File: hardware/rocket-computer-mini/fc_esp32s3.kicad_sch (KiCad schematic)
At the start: 35 parts, among them SW2 R-667995, U32 ESP32-S3RH2, U33 GD25Q128ESIG, Y3 ABS07-32.768KHZ-T, Y4 ECS-400-10-37B2-CKY-TR

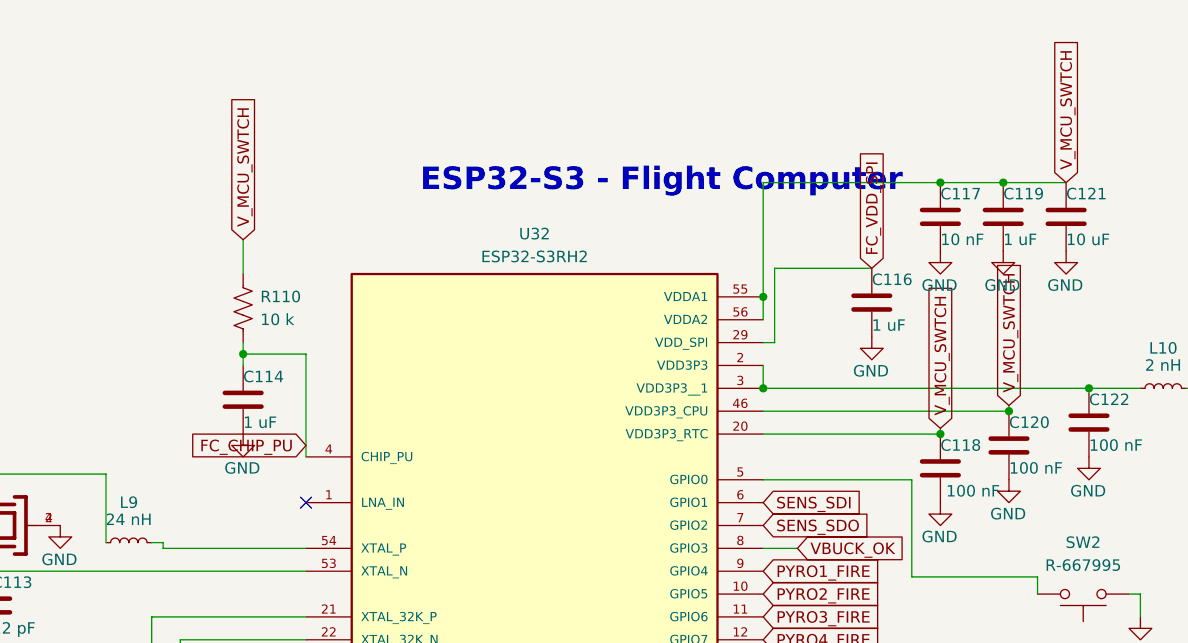
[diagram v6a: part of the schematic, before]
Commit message: rocket-computer-mini: place the board and re-sync the netlist
Placement of all 214 footprints — the import scatter block that sat at x>130 is
gone and everything now falls within x 73.2-124.5 / y 103.7-170.1 mm. The
22.5 x 69.5 mm outline is restored on Edge.Cuts, having gone missing between
0e0f2d5 and 7ad7508 (the pack-direct pyro/supercap WIP commit), which left the
file with no board boundary at all in between.

The stale P4-era track stubs are cleared, and the board is re-synced from the
schematic so its net names finally match: CAP_ACTIVE -> VBUCK_OK and
ARM_CLK -> WDT_PET, plus FC_ARM, OC_ARM_EN and the rest of the arm and TPS61094
hold-up nets. Before this the board file lagged the schematic by two reworks —
9 schematic nets had no PCB counterpart and 3 PCB nets no longer existed — and
kicad-cli pcb drc --schematic-parity did not flag it, because it reconciles
footprints rather than stale net strings.

Not a finished layout: 0 routed segments, 2 vias, 12 zones. DRC reports 103
violations and 372 unconnected pads, which is the expected shape for a placed,
unrouted board.

Taken from the owner's working tree and committed here so the I2S net rename
that follows could be applied on top of it rather than conflicting with it.

Co-Authored-By: Claude Opus 5 <noreply@anthropic.com>
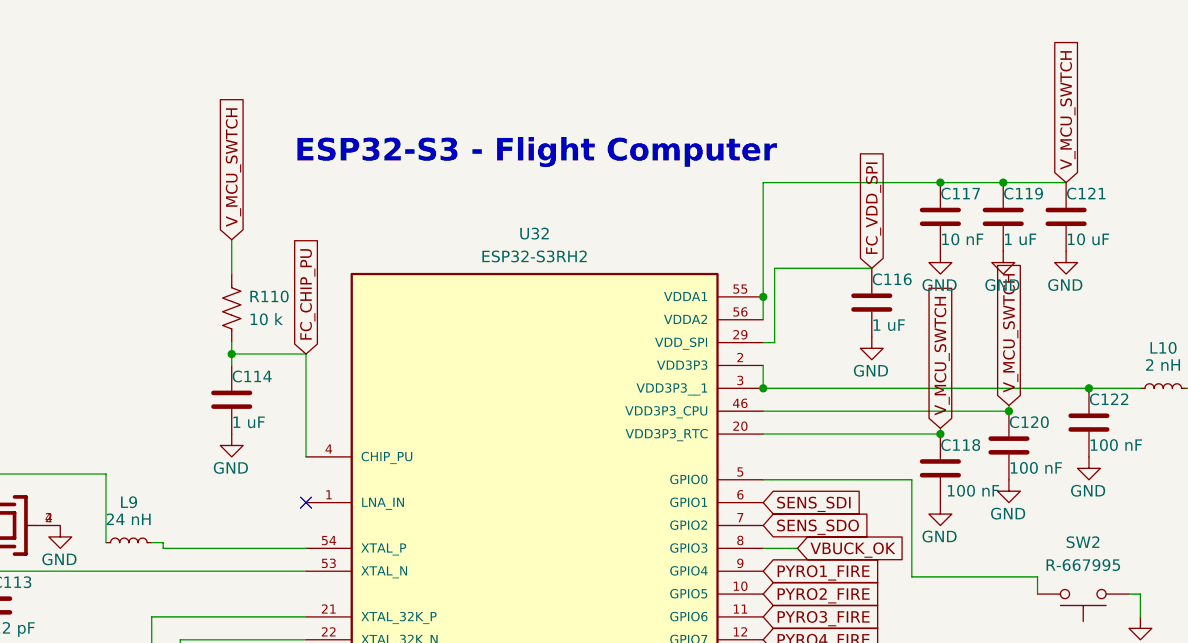
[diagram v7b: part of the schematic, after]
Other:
- moved on the sheet: C114, R110
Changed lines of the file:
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@@
 	(text "ESP32-S3 - Flight Computer"
 		(exclude_from_sim no)
-		(at 151.765 33.02 0)
+		(at 137.795 29.845 0)
 		(effects
 			(font
@@
 	)
 	(junction
-		(at 132.08 50.8)
-		(diameter 0)
-		(color 0 0 0 0)
-	)
-	(junction
 		(at 248.92 54.61)
 		(diameter 0)
@@
 		(color 0 0 0 0)
 	)
+	(junction
+		(at 130.81 50.8)
+		(diameter 0)
+		(color 0 0 0 0)
+	)
 	(no_connect
 		(at 139.065 67.31)
@@
 	(wire
 		(pts
+			(xy 133.985 100.33) (xy 139.065 100.33)
+		)
+		(stroke
+			(width 0)
+			(type default)
+		)
+	)
+	(wire
+		(pts
 			(xy 55.88 118.745) (xy 62.865 118.745)
 		)
@@
 	(wire
 		(pts
-			(xy 132.08 38.1) (xy 132.08 41.91)
+			(xy 130.81 38.1) (xy 130.81 41.91)
 		)
 		(stroke
@@
 	(wire
 		(pts
+			(xy 130.81 50.8) (xy 139.065 50.8)
+		)
+		(stroke
+			(width 0)
+			(type default)
+		)
+	)
+	(wire
+		(pts
 			(xy 189.865 133.35) (xy 193.675 133.35)
 		)
@@
 	(wire
 		(pts
-			(xy 132.08 50.8) (xy 132.08 52.07)
+			(xy 130.81 50.8) (xy 130.81 52.07)
 		)
 		(stroke
@@
 	(wire
 		(pts
+			(xy 139.065 50.8) (xy 139.065 62.23)
+		)
+		(stroke
+			(width 0)
+			(type default)
+		)
+	)
+	(wire
+		(pts
 			(xy 240.03 54.61) (xy 248.92 54.61)
 		)
@@
 	(wire
 		(pts
-			(xy 132.08 49.53) (xy 132.08 50.8)
+			(xy 130.81 49.53) (xy 130.81 50.8)
 		)
 		(stroke
@@
 	(wire
 		(pts
-			(xy 139.065 50.8) (xy 132.08 50.8)
-		)
-		(stroke
-			(width 0)
-			(type default)
-		)
-	)
-	(wire
-		(pts
 			(xy 116.84 64.135) (xy 116.84 71.755)
 		)
@@
 	(wire
 		(pts
-			(xy 139.065 62.23) (xy 139.065 50.8)
-		)
-		(stroke
-			(width 0)
-			(type default)
-		)
-	)
-	(wire
-		(pts
 			(xy 139.065 80.01) (xy 121.92 80.01)
 		)
@@
 		)
 	)
+	(global_label "FC_CHIP_PU"
+		(shape input)
+		(at 139.065 50.8 90)
+		(fields_autoplaced yes)
+		(effects
+			(font
+				(size 1.27 1.27)
+			)
+			(justify left)
+		)
+		(property "Intersheetrefs" "${INTERSHEET_REFS}"
+			(at 139.065 36.4452 90)
+			(hide yes)
+			(show_name no)
+			(do_not_autoplace no)
+			(effects
+				(font
+					(size 1.27 1.27)
+				)
+				(justify left)
+			)
+		)
+	)
+	(global_label "FC_ARM"
+		(shape input)
+		(at 133.985 100.33 180)
+		(fields_autoplaced yes)
+		(effects
+			(font
+				(size 1.27 1.27)
+			)
+			(justify right)
+		)
+		(property "Intersheetrefs" "${INTERSHEET_REFS}"
+			(at 133.985 100.33 0)
+			(hide yes)
+			(show_name no)
+			(do_not_autoplace no)
+			(effects
+				(font
+					(size 1.27 1.27)
+				)
+				(justify right)
+			)
+		)
+	)
 	(global_label "FC_D-"
 		(shape input)
@@
 	(global_label "V_MCU_SWTCH"
 		(shape input)
-		(at 132.08 38.1 90)
+		(at 130.81 38.1 90)
 		(fields_autoplaced yes)
 		(effects
@@
 		)
 		(property "Intersheetrefs" "${INTERSHEET_REFS}"
-			(at 132.08 21.81 90)
+			(at 130.81 21.81 90)
 			(hide yes)
 			(show_name no)
@@
 	(symbol
 		(lib_id "Device:R_US")
-		(at 132.08 45.72 0)
+		(at 130.81 45.72 0)
 		(unit 1)
 		(body_style 1)
@@
 		(fields_autoplaced yes)
 		(property "Reference" "R110"
-			(at 133.985 44.4499 0)
+			(at 132.715 44.4499 0)
 			(show_name no)
 			(do_not_autoplace no)
@@
 		)
 		(property "Value" "10 k"
-			(at 133.985 46.9899 0)
+			(at 132.715 46.9899 0)
 			(show_name no)
 			(do_not_autoplace no)
@@
 		)
 		(property "Footprint" "Resistor_SMD:R_0402_1005Metric"
-			(at 133.096 45.974 90)
+			(at 131.826 45.974 90)
 			(hide yes)
 			(show_name no)
@@
 		)
 		(property "Datasheet" ""
-			(at 132.08 45.72 0)
+			(at 130.81 45.72 0)
 			(hide yes)
 			(show_name no)
@@
 		)
 		(property "Description" "Resistor, US symbol"
-			(at 132.08 45.72 0)
+			(at 130.81 45.72 0)
 			(hide yes)
 			(show_name no)
@@
 		)
 		(property "MPN" "RC0402FR-0710KL"
-			(at 132.08 45.72 0)
+			(at 130.81 45.72 0)
 			(hide yes)
 			(show_name no)
@@
 		)
 		(property "Mfr" "Yageo"
-			(at 132.08 45.72 0)
+			(at 130.81 45.72 0)
 			(hide yes)
 			(show_name no)
@@
 	(symbol
 		(lib_id "Device:C")
-		(at 132.08 55.88 0)
+		(at 130.81 55.88 0)
 		(unit 1)
 		(body_style 1)
@@
 		(dnp no)
 		(property "Reference" "C114"
-			(at 132.08 53.34 0)
+			(at 130.81 53.34 0)
 			(show_name no)
 			(do_not_autoplace no)
@@
 		)
 		(property "Value" "1 uF"
-			(at 132.08 58.42 0)
+			(at 130.81 58.42 0)
 			(show_name no)
 			(do_not_autoplace no)
@@
 		)
 		(property "Footprint" "Capacitor_SMD:C_0402_1005Metric"
-			(at 133.0452 59.69 0)
+			(at 131.7752 59.69 0)
 			(hide yes)
 			(show_name no)
@@
 		)
 		(property "Datasheet" ""
-			(at 132.08 55.88 0)
+			(at 130.81 55.88 0)
 			(hide yes)
 			(show_name no)
@@
 		)
 		(property "Description" "Unpolarized capacitor"
-			(at 132.08 55.88 0)
+			(at 130.81 55.88 0)
 			(hide yes)
 			(show_name no)
@@
 		)
 		(property "MPN" "CL05A105KO5NNNC"
-			(at 132.08 55.88 0)
+			(at 130.81 55.88 0)
 			(hide yes)
 			(show_name no)
@@
 		)
 		(property "Mfr" "Samsung"
-			(at 132.08 55.88 0)
+			(at 130.81 55.88 0)
 			(hide yes)
 			(show_name no)
@@
 	(symbol
 		(lib_id "power:GND")
-		(at 132.08 59.69 0)
+		(at 130.81 59.69 0)
 		(unit 1)
 		(body_style 1)
@@
 		(dnp no)
 		(property "Reference" "#PWR0311"
-			(at 132.08 66.04 0)
+			(at 130.81 66.04 0)
 			(hide yes)
 			(show_name no)
@@
 		)
 		(property "Value" "GND"
-			(at 133.985 63.5 0)
+			(at 132.715 63.5 0)
 			(show_name no)
 			(do_not_autoplace no)
@@
 		)
 		(property "Footprint" ""
-			(at 132.08 59.69 0)
+			(at 130.81 59.69 0)
 			(hide yes)
 			(show_name no)
@@
 		)
 		(property "Datasheet" ""
-			(at 132.08 59.69 0)
+			(at 130.81 59.69 0)
 			(hide yes)
 			(show_name no)
@@
 		)
 		(property "Description" "Power symbol creates a global label with name \"GND\" , ground"
-			(at 132.08 59.69 0)
+			(at 130.81 59.69 0)
 			(hide yes)
 			(show_name no)
@@
 			)
 		)
-	)
-	(wire
-		(pts
-			(xy 133.985 100.33) (xy 139.065 100.33)
-		)
-		(stroke
-			(width 0)
-			(type default)
-		)
-	)
-	(global_label "FC_ARM"
-		(shape input)
-		(at 133.985 100.33 180)
-		(fields_autoplaced yes)
-		(effects
-			(font
-				(size 1.27 1.27)
-			)
-			(justify right)
-		)
-		(property "Intersheetrefs" "${INTERSHEET_REFS}"
-			(at 133.985 100.33 0)
-			(hide yes)
-			(show_name no)
-			(do_not_autoplace no)
-			(effects
-				(font
-					(size 1.27 1.27)
-				)
-				(justify right)
-			)
-		)
-	)
-	(global_label "FC_CHIP_PU"
-		(shape input)
-		(at 139.065 60.96 180)
-		(fields_autoplaced yes)
-		(effects
-			(font
-				(size 1.27 1.27)
-			)
-			(justify right)
-		)
-		(property "Intersheetrefs" "${INTERSHEET_REFS}"
-			(at 139.065 60.96 0)
-			(hide yes)
-			(show_name no)
-			(do_not_autoplace no)
-			(effects
-				(font
-					(size 1.27 1.27)
-				)
-				(justify right)
-			)
-		)

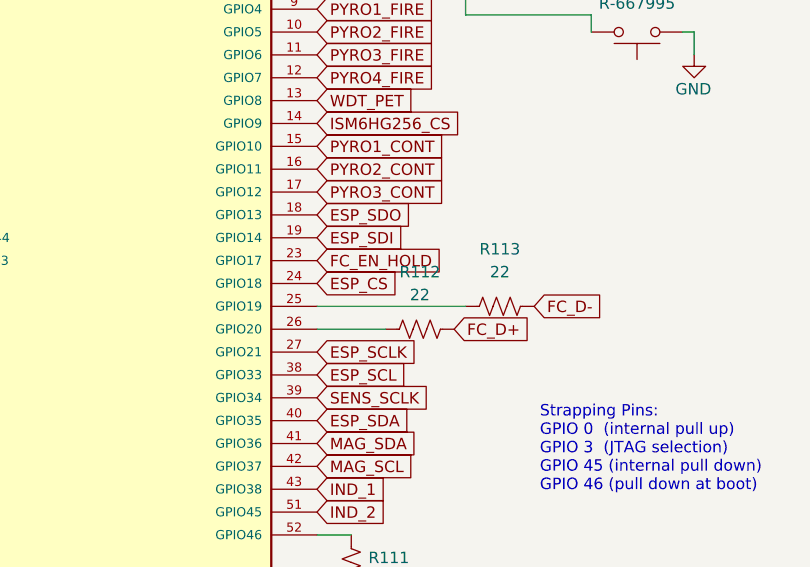
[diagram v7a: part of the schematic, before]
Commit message: rocket-computer-mini: I2S net rename on top of the layout pass
Applies the same four renames to the mini that the previous commit applied to
rocket-computer, now rebased onto the placed board rather than conflicting with
it: ESP_SCLK -> ESP_I2S_BCLK, ESP_CS -> ESP_I2S_WS, ESP_SDO -> ESP_I2S_SD,
ESP_SDI -> ESP_I2S_FSYNC. ESP_SCL/ESP_SDA keep their names.

Also updates the GPIO3 note on the out-computer sheet to match, and rewrites the
README status block against the board as it now stands instead of the state two
reworks ago: 214 footprints placed inside x 73.2-124.5 / y 103.7-170.1, the
22.5 x 69.5 mm outline restored on Edge.Cuts, net names re-synced with the
schematic, nothing routed yet.

That last point is worth recording. Before this layout pass the board file
lagged the schematic by two reworks - 9 schematic nets had no PCB counterpart
and 3 PCB nets no longer existed - and kicad-cli pcb drc --schematic-parity did
not flag it, because it reconciles footprints rather than stale net strings. A
pin-map audit taken from the board file instead of a netlist export produced
three wrong findings as a result. The README now says to export the netlist.

Verification against the placed board: netlist fingerprints diff to exactly the
four renames with identical node lists; 214 components and 205 nets unchanged;
ERC 40 -> 40; DRC 103 -> 103 with an identical violation-type histogram, and the
sorted rename-normalised reports are byte-identical. rocket-computer still
reports its own 19. check_board_parity now finds the mini complete, so its
exemption in tools/check_board_parity.py can be dropped once the layout settles.

Co-Authored-By: Claude Opus 5 <noreply@anthropic.com>
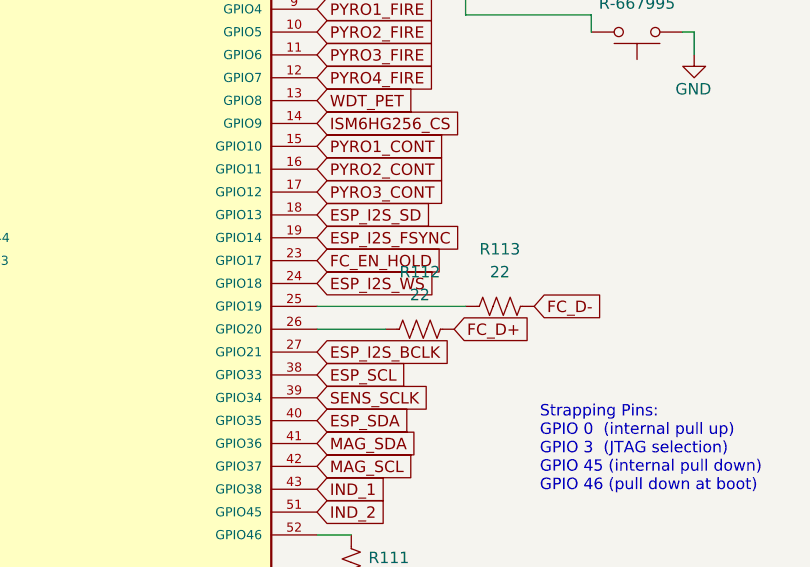
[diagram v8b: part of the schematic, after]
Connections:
- net ESP_CS renamed ESP_I2S_WS
- net ESP_SCLK renamed ESP_I2S_BCLK
- net ESP_SDI renamed ESP_I2S_FSYNC
- net ESP_SDO renamed ESP_I2S_SD
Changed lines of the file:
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@@
 		)
 	)
-	(global_label "ESP_SDO"
+	(global_label "ESP_I2S_SD"
 		(shape input)
 		(at 189.865 97.79 0)
@@
 		)
 	)
-	(global_label "ESP_SDI"
+	(global_label "ESP_I2S_FSYNC"
 		(shape input)
 		(at 189.865 100.33 0)
@@
 		)
 	)
-	(global_label "ESP_CS"
+	(global_label "ESP_I2S_WS"
 		(shape input)
 		(at 189.865 105.41 0)
@@
 		)
 	)
-	(global_label "ESP_SCLK"
+	(global_label "ESP_I2S_BCLK"
 		(shape input)
 		(at 189.865 113.03 0)
